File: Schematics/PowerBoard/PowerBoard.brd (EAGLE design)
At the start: 143.2 x 109.2 mm, 22 parts

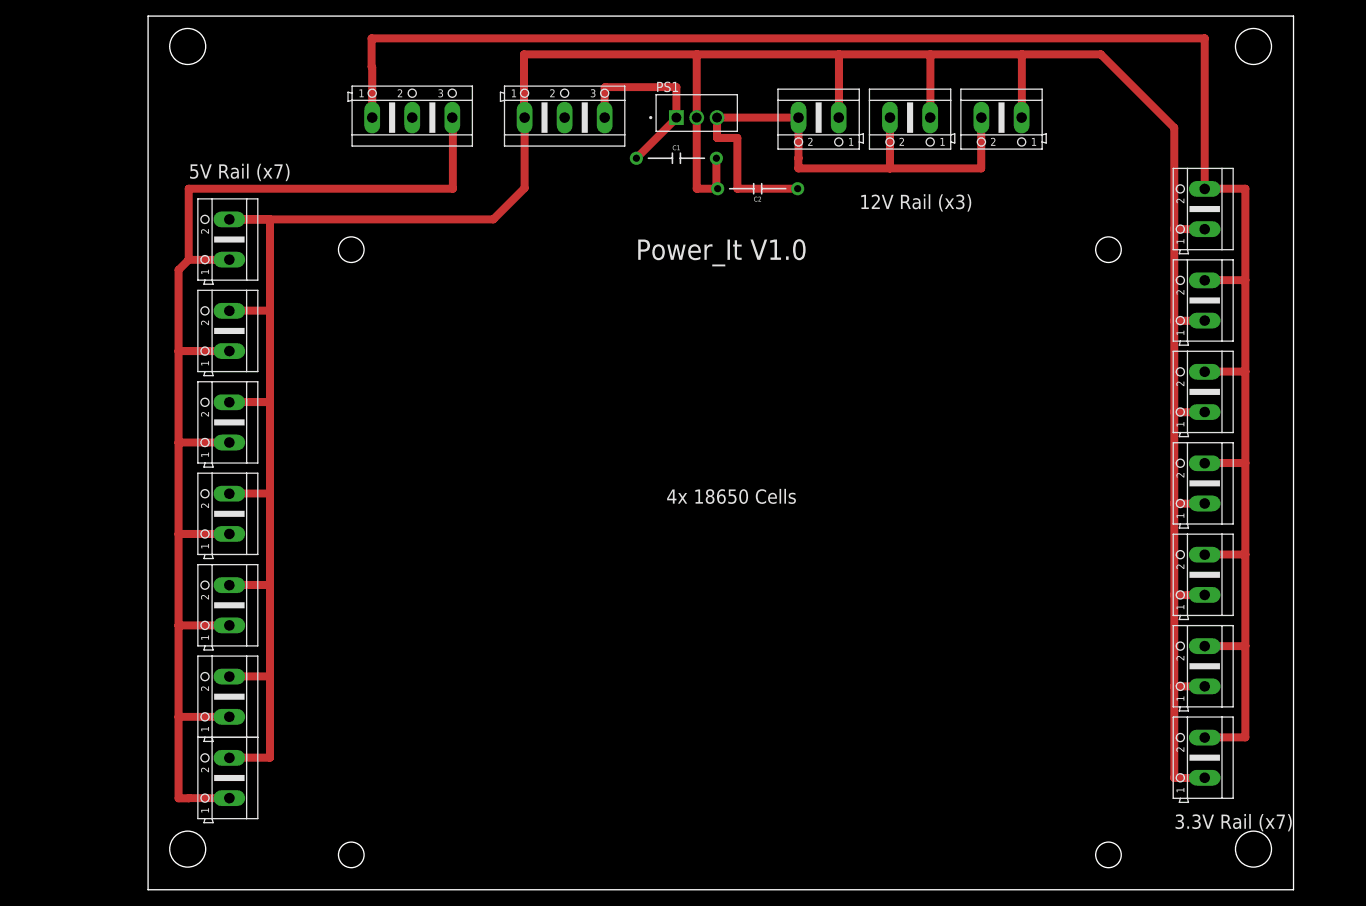
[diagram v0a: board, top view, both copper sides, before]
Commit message: Refactored Power PCB
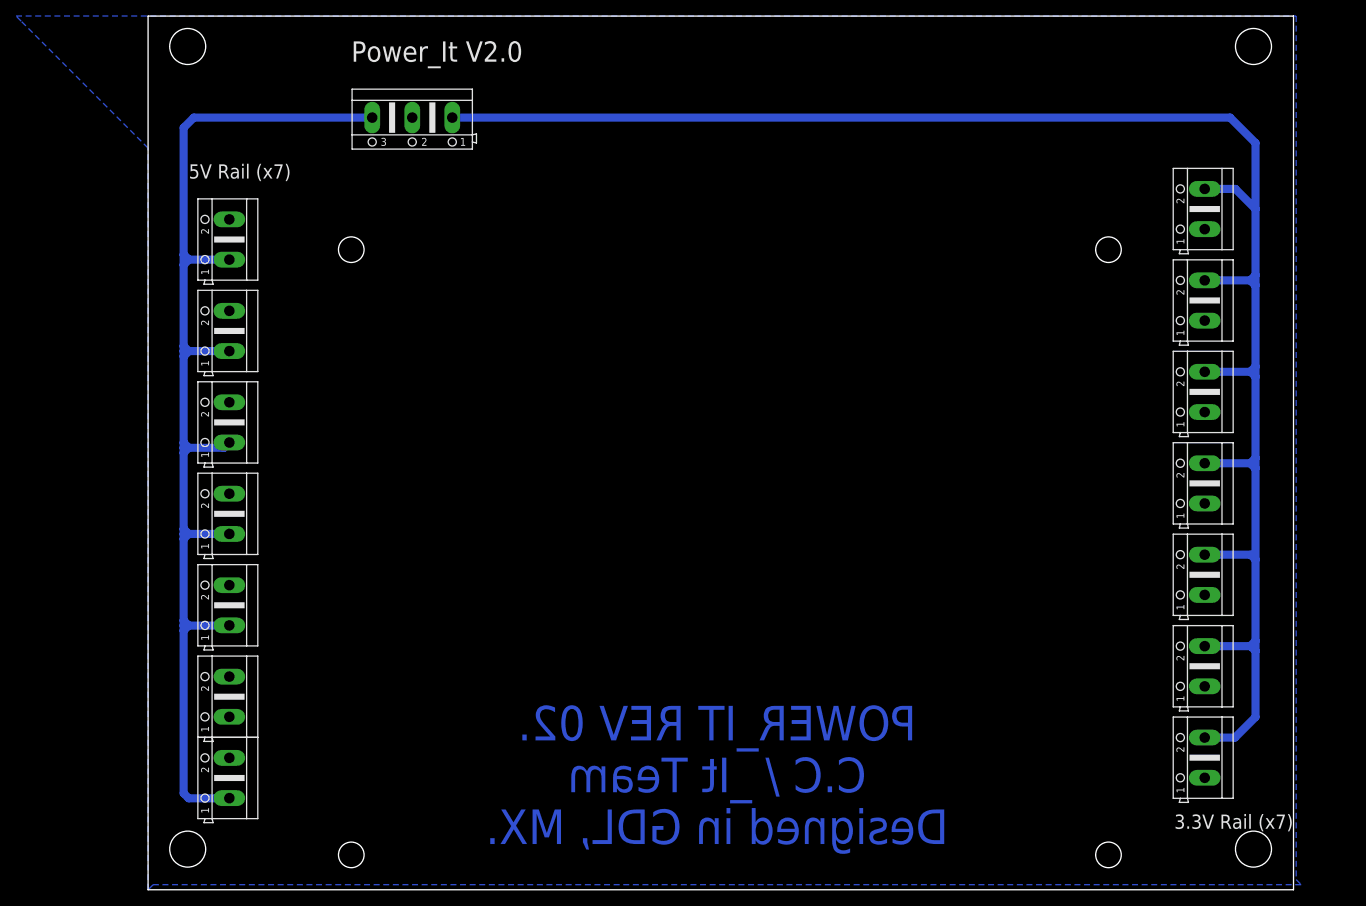
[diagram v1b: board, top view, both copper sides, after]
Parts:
- removed C1, C2: 10nF, SparkFun-Capacitors:CAP-PTH-10MM
- removed PS1: LM7812, LM7812:VREG_LM7812
- removed X17, X18, X19: (no value), con-ptr500:AK500/2
- removed X2: (no value), con-ptr500:AK500/3
- turned X1 to 180 degrees
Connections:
- net N$3 renamed 5V
- net N$5 renamed 3.3V
- removed net N$1: C1.1, PS1.1, X2.3
- removed net N$2: C1.2, C2.2, PS1.2, X10.1, X11.1, X12.1, X13.1, X14.1, X15.1, X16.1, X17.1, X18.1, X19.1, X2.1, X3.2, X4.2, X5.2, X6.2, X7.2, X8.2, X9.2
- removed net N$4: C2.1, PS1.3, X17.2, X18.2, X19.2
- new net GND: X1.2, X10.1, X11.1, X12.1, X13.1, X14.1, X15.1, X16.1, X3.2, X4.2, X5.2, X6.2, X7.2, X8.2, X9.2
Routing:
- net N$2: track 398.3 -> 0.00 mm
- net N$4: track 71.1 -> 0.00 mm
- net N$1: track 23.7 -> 0.00 mm
- net 5V: track 163.2 -> 150.5 mm
- net 3.3V: track 237.1 -> 225.0 mm
- added copper zone on layer 16, net GND
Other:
- board text added: "POWER_IT REV 02. C.C / _It Team Designed in GDL, MX."
- board text added: "Power_It V2.0"
- board text removed: "12V Rail (x3)"
- board text removed: "4x 18650 Cells"
- board text removed: "Power_It V1.0"
